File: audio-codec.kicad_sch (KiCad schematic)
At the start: 25 parts, among them J1 AudioJack2_Ground, J2 AudioJack2_Ground, U4 XTAC5112IRGER

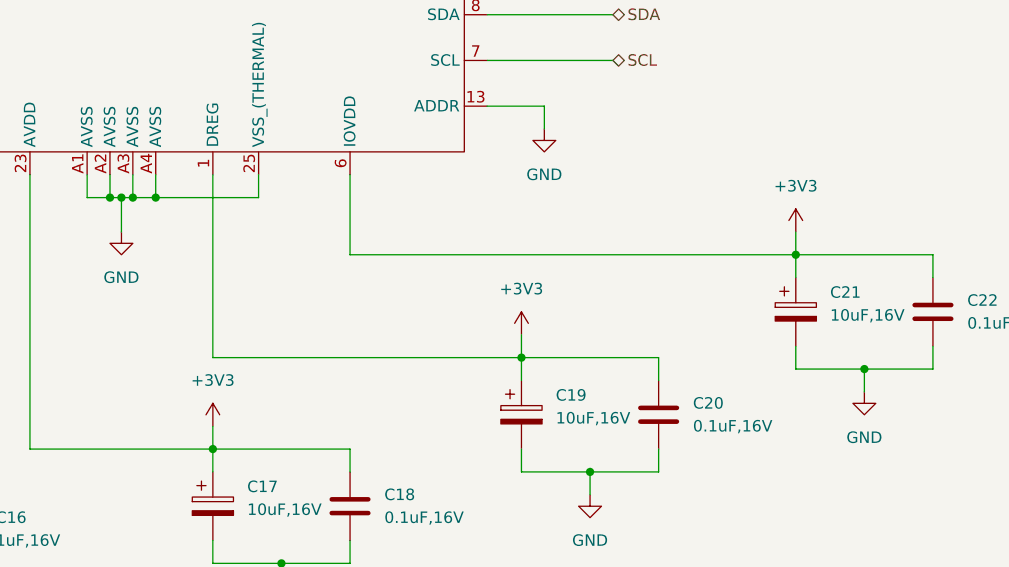
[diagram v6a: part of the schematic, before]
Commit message: Changed codec rail to 3V3_Osc and addressed all DRCs (including previous overrides)
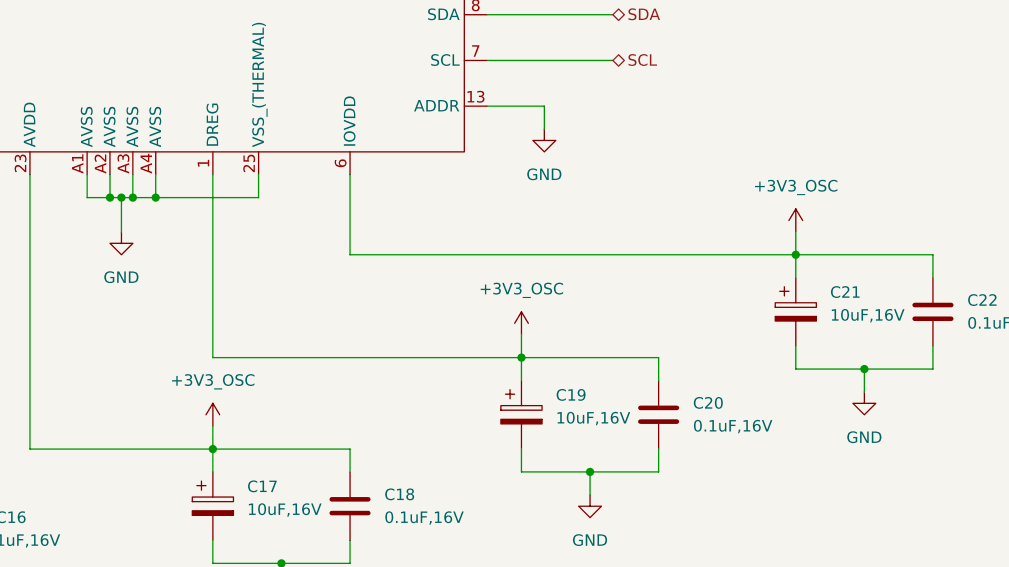
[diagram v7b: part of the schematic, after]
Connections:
- net +3V3 renamed +3V3_OSC
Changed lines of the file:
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@@
+	)
+	(symbol
+		(lib_id "power:+3V3")
+		(at 165.1 137.16 0)
+		(unit 1)
+		(exclude_from_sim no)
+		(in_bom yes)
+		(on_board yes)
+		(dnp no)
+		(fields_autoplaced yes)
+		(property "Reference" "#PWR012"
+			(at 165.1 140.97 0)
+			(effects
+				(font
+					(size 1.27 1.27)
+				)
+				(hide yes)
+			)
+		)
+		(property "Value" "+3V3_OSC"
+			(at 165.1 132.08 0)
+			(effects
+				(font
+					(size 1.27 1.27)
+				)
+			)
+		)
+		(property "Footprint" ""
+			(at 165.1 137.16 0)
+			(effects
+				(font
+					(size 1.27 1.27)
+				)
+				(hide yes)
+			)
+		)
+		(property "Datasheet" ""
+			(at 165.1 137.16 0)
+			(effects
+				(font
+					(size 1.27 1.27)
+				)
+				(hide yes)
+			)
+		)
+		(property "Description" "Power symbol creates a global label with name \"+3V3\""
+			(at 165.1 137.16 0)
+			(effects
+				(font
+					(size 1.27 1.27)
+				)
+				(hide yes)
+			)
+		)
+		(pin "1"
+		)
+		(instances
+			(project "jkembedded-audio-board"
+				(path "/df100556-b288-4cb1-b69f-c0734132cb90/f904953f-335e-4512-b297-b8d4a411c7e1"
+					(reference "#PWR012")
+					(unit 1)
+				)
+			)
+		)
 	)
 	(symbol
@@
 	)
 	(symbol
+		(lib_id "power:+3V3")
+		(at 199.39 127 0)
+		(unit 1)
+		(exclude_from_sim no)
+		(in_bom yes)
+		(on_board yes)
+		(dnp no)
+		(fields_autoplaced yes)
+		(property "Reference" "#PWR09"
+			(at 199.39 130.81 0)
+			(effects
+				(font
+					(size 1.27 1.27)
+				)
+				(hide yes)
+			)
+		)
+		(property "Value" "+3V3_OSC"
+			(at 199.39 121.92 0)
+			(effects
+				(font
+					(size 1.27 1.27)
+				)
+			)
+		)
+		(property "Footprint" ""
+			(at 199.39 127 0)
+			(effects
+				(font
+					(size 1.27 1.27)
+				)
+				(hide yes)
+			)
+		)
+		(property "Datasheet" ""
+			(at 199.39 127 0)
+			(effects
+				(font
+					(size 1.27 1.27)
+				)
+				(hide yes)
+			)
+		)
+		(property "Description" "Power symbol creates a global label with name \"+3V3\""
+			(at 199.39 127 0)
+			(effects
+				(font
+					(size 1.27 1.27)
+				)
+				(hide yes)
+			)
+		)
+		(pin "1"
+		)
+		(instances
+			(project "jkembedded-audio-board"
+				(path "/df100556-b288-4cb1-b69f-c0734132cb90/f904953f-335e-4512-b297-b8d4a411c7e1"
+					(reference "#PWR09")
+					(unit 1)
+				)
+			)
+		)
+	)
+	(symbol
 		(lib_id "power:GND")
 		(at 74.93 120.65 0)
@@
 				(path "/df100556-b288-4cb1-b69f-c0734132cb90/f904953f-335e-4512-b297-b8d4a411c7e1"
 					(reference "#PWR033")
-					(unit 1)
-				)
-			)
-		)
-	)
-	(symbol
-		(lib_id "power:+3V3")
-		(at 165.1 137.16 0)
-		(unit 1)
-		(exclude_from_sim no)
-		(in_bom yes)
-		(on_board yes)
-		(dnp no)
-		(fields_autoplaced yes)
-		(property "Reference" "#PWR035"
-			(at 165.1 140.97 0)
-			(effects
-				(font
-					(size 1.27 1.27)
-				)
-				(hide yes)
-			)
-		)
-		(property "Value" "+3V3"
-			(at 165.1 132.08 0)
-			(effects
-				(font
-					(size 1.27 1.27)
-				)
-			)
-		)
-		(property "Footprint" ""
-			(at 165.1 137.16 0)
-			(effects
-				(font
-					(size 1.27 1.27)
-				)
-				(hide yes)
-			)
-		)
-		(property "Datasheet" ""
-			(at 165.1 137.16 0)
-			(effects
-				(font
-					(size 1.27 1.27)
-				)
-				(hide yes)
-			)
-		)
-		(property "Description" "Power symbol creates a global label with name \"+3V3\""
-			(at 165.1 137.16 0)
-			(effects
-				(font
-					(size 1.27 1.27)
-				)
-				(hide yes)
-			)
-		)
-		(pin "1"
-		)
-		(instances
-			(project ""
-				(path "/df100556-b288-4cb1-b69f-c0734132cb90/f904953f-335e-4512-b297-b8d4a411c7e1"
-					(reference "#PWR035")
 					(unit 1)
 				)
@@
 				(path "/df100556-b288-4cb1-b69f-c0734132cb90/f904953f-335e-4512-b297-b8d4a411c7e1"
 					(reference "#PWR036")
+					(unit 1)
+				)
+			)
+		)
+	)
+	(symbol
+		(lib_id "power:+3V3")
+		(at 229.87 115.57 0)
+		(unit 1)
+		(exclude_from_sim no)
+		(in_bom yes)
+		(on_board yes)
+		(dnp no)
+		(fields_autoplaced yes)
+		(property "Reference" "#PWR08"
+			(at 229.87 119.38 0)
+			(effects
+				(font
+					(size 1.27 1.27)
+				)
+				(hide yes)
+			)
+		)
+		(property "Value" "+3V3_OSC"
+			(at 229.87 110.49 0)
+			(effects
+				(font
+					(size 1.27 1.27)
+				)
+			)
+		)
+		(property "Footprint" ""
+			(at 229.87 115.57 0)
+			(effects
+				(font
+					(size 1.27 1.27)
+				)
+				(hide yes)
+			)
+		)
+		(property "Datasheet" ""
+			(at 229.87 115.57 0)
+			(effects
+				(font
+					(size 1.27 1.27)
+				)
+				(hide yes)
+			)
+		)
+		(property "Description" "Power symbol creates a global label with name \"+3V3\""
+			(at 229.87 115.57 0)
+			(effects
+				(font
+					(size 1.27 1.27)
+				)
+				(hide yes)
+			)
+		)
+		(pin "1"
+		)
+		(instances
+			(project "jkembedded-audio-board"
+				(path "/df100556-b288-4cb1-b69f-c0734132cb90/f904953f-335e-4512-b297-b8d4a411c7e1"
+					(reference "#PWR08")
 					(unit 1)
 				)
@@
 	)
 	(symbol
-		(lib_id "power:+3V3")
-		(at 229.87 115.57 0)
-		(unit 1)
-		(exclude_from_sim no)
-		(in_bom yes)
-		(on_board yes)
-		(dnp no)
-		(fields_autoplaced yes)
-		(property "Reference" "#PWR040"
-			(at 229.87 119.38 0)
-			(effects
-				(font
-					(size 1.27 1.27)
-				)
-				(hide yes)
-			)
-		)
-		(property "Value" "+3V3"
-			(at 229.87 110.49 0)
-			(effects
-				(font
-					(size 1.27 1.27)
-				)
-			)
-		)
-		(property "Footprint" ""
-			(at 229.87 115.57 0)
-			(effects
-				(font
-					(size 1.27 1.27)
-				)
-				(hide yes)
-			)
-		)
-		(property "Datasheet" ""
-			(at 229.87 115.57 0)
-			(effects
-				(font
-					(size 1.27 1.27)
-				)
-				(hide yes)
-			)
-		)
-		(property "Description" "Power symbol creates a global label with name \"+3V3\""
-			(at 229.87 115.57 0)
-			(effects
-				(font
-					(size 1.27 1.27)
-				)
-				(hide yes)
-			)
-		)
-		(pin "1"
-		)
-		(instances
-			(project "jkembedded-audio-board"
-				(path "/df100556-b288-4cb1-b69f-c0734132cb90/f904953f-335e-4512-b297-b8d4a411c7e1"
-					(reference "#PWR040")
-					(unit 1)
-				)
-			)
-		)
-	)
-	(symbol
 		(lib_id "Device:C")
 		(at 92.71 91.44 90)
@@
 					(unit 1)
 				)
-			)
-		)
-	)
-	(symbol
-		(lib_id "power:+3V3")
-		(at 199.39 127 0)
-		(unit 1)
-		(exclude_from_sim no)
-		(in_bom yes)
-		(on_board yes)
-		(dnp no)
-		(fields_autoplaced yes)
-		(property "Reference" "#PWR038"
-			(at 199.39 130.81 0)
-			(effects
-				(font
-					(size 1.27 1.27)
-				)
-				(hide yes)
-			)
-		)
-		(property "Value" "+3V3"
-			(at 199.39 121.92 0)
-			(effects
-				(font
-					(size 1.27 1.27)
-				)
-			)
-		)
-		(property "Footprint" ""
-			(at 199.39 127 0)
-			(effects
-				(font
-					(size 1.27 1.27)
-				)
-				(hide yes)
-			)
-		)
-		(property "Datasheet" ""
-			(at 199.39 127 0)
-			(effects
-				(font
-					(size 1.27 1.27)
-				)
-				(hide yes)
-			)
-		)
-		(property "Description" "Power symbol creates a global label with name \"+3V3\""
-			(at 199.39 127 0)
-			(effects
-				(font
-					(size 1.27 1.27)
-				)
-				(hide yes)
-			)
-		)
-		(pin "1"
-		)
-		(instances
-			(project "jkembedded-audio-board"
-				(path "/df100556-b288-4cb1-b69f-c0734132cb90/f904953f-335e-4512-b297-b8d4a411c7e1"
-					(reference "#PWR038")
-					(unit 1)
-				)
